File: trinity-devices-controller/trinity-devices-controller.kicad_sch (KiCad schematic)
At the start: 90 parts, among them IC1 LM25145RGYR, IC2 MCP2562, J1 xh2pin, J10 xh2pin, J11 Conn_01x03, J12 Conn_01x03, J13 Conn_01x03, J2 xh2pin, J3 Conn_01x01_Pin, J4 Conn_01x01_Pin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

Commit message: 配置、配線完了
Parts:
- added C32: 0.1uf, Capacitor_SMD:C_0603_1608Metric_Pad1.08x0.95mm_HandSolder, symbol Device:C
- added D10, D11, D12, D5, D6, D7, D8, D9: LED, LED_SMD:LED_0603_1608Metric_Pad1.05x0.95mm_HandSolder, symbol Device:LED
- added J14: Conn_01x02, Connector_AMASS:AMASS_XT30UPB-M_1x02_P5.0mm_Vertical, symbol Connector_Generic:Conn_01x02
- added J15: Conn_01x03, Connector_JST:JST_XH_B3B-XH-A_1x03_P2.50mm_Vertical, symbol Connector_Generic:Conn_01x03
- added R27, R28, R29, R30, R31: 10k, Resistor_SMD:R_0603_1608Metric_Pad0.98x0.95mm_HandSolder, symbol Device:R
- added R32, R33, R34, R35, R36, R37, R38, R39: 1k, Resistor_SMD:R_0603_1608Metric_Pad0.98x0.95mm_HandSolder, symbol Device:R
- J1, J10, J2, J9: footprint Connector_JST:JST_XH_S2B-XH-A_1x02_P2.50mm_Horizontal -> Connector_JST:JST_XH_B2B-XH-A_1x02_P2.50mm_Vertical
- J11, J12, J13: footprint Connector_JST:JST_XH_S3B-XH-A_1x03_P2.50mm_Horizontal -> Connector_JST:JST_XH_B3B-XH-A_1x03_P2.50mm_Vertical
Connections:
- net +12V: now also J11.2 (Pin_2), J12.2 (Pin_2), J13.2 (Pin_2), J14.2 (Pin_2), J15.2 (Pin_2); no longer J11.3 (Pin_3), J12.3 (Pin_3), J13.3 (Pin_3)
- net GND: now also C32.2, J14.1 (Pin_1), J15.1 (Pin_1), R27.1, R28.1, R29.1, R30.1
- net GNDD: now also D10.1 (K), D11.1 (K), D12.1 (K), D5.1 (K), D6.1 (K), D7.1 (K), D8.1 (K), D9.1 (K), R31.2
- net IN1: now also U3.10 (PA5), R32.1; no longer U3.9 (PA4)
- net IN2: now also U3.9 (PA4), R33.1; no longer U3.10 (PA5)
- net IN3: now also R34.1
- net IN4: now also R35.1
- net PWM1: now also J11.3 (Pin_3), U8.11 (OUTD), R27.2; no longer J11.2 (Pin_2), U8.14 (OUTA)
- net PWM2: now also J12.3 (Pin_3), U8.12 (OUTC), R28.2; no longer J12.2 (Pin_2), U8.13 (OUTB)
- net PWM3: now also J13.3 (Pin_3), U8.13 (OUTB), R29.2; no longer J13.2 (Pin_2), U8.12 (OUTC)
- net TIM2_CH1: now also U8.6 (IND), R31.1, R39.1; no longer R26.1, U8.3 (INA)
- net TIM2_CH2: now also R24.1, U8.5 (INC), R38.1; no longer R25.1, U8.4 (INB)
- net TIM2_CH3: now also R25.1, U8.4 (INB), R37.1; no longer R24.1, U8.5 (INC)
- net VCC: now also C32.1
- net at R18.2: now also U1.3; no longer U1.5
- net at R3.1, R5.1: now also U1.11; no longer U1.15
- net at R2.2: now also U1.7; no longer U1.3
- net at R4.1, R6.1: now also U1.9; no longer U1.13
- net at U1.1: now also R21.2; no longer R1.2
- net at R19.1, R20.1: now also U1.13; no longer U1.11
- net at C3.2, C5.1, IC1.5 (FB)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: now also R14.2; no longer C6.2
- net at C5.2, IC1.4 (COMP): now also C6.1; no longer R14.1
- net TIM2_CH4: now reaches U3.8 (PA3)
- net TIM2_CH4: now also R26.1, U8.3 (INA), R36.1
- net at R22.1, R23.1: now also U1.15; no longer U1.9
- new net: D8.2 (A), R35.2
- new net: D5.2 (A), R32.2
- new net: D6.2 (A), R33.2
- new net: D10.2 (A), R37.2
- new net: D11.2 (A), R38.2
- new net: D7.2 (A), R34.2
- new net: C6.2, R14.1
- new net: D9.2 (A), R36.2
- new net: D12.2 (A), R39.2
- new net: R1.2, U1.5
- new net PWM4: J15.3 (Pin_3), R30.2, U8.14 (OUTA)
- no-connect marks 17 -> 14
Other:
- note added: "電源入出力"
- note removed: "電源入力"
- moved on the sheet: C6, J11, J12, J13, J3, J4, R14, R24, R25, R26, U1A, U1B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

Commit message: ビア以外完成
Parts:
- added D13, D14, D15, D16, D17: LED, LED_SMD:LED_0603_1608Metric_Pad1.05x0.95mm_HandSolder, symbol Device:LED
- added R40, R41, R42, R43, R44: 1k, Resistor_SMD:R_0603_1608Metric_Pad0.98x0.95mm_HandSolder, symbol Device:R
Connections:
- net +12V: now also R40.1
- net +3.3V: now also R43.1
- net +5P: now also R41.1
- net +5V: now also R44.1
- net GND: now also D13.1 (K), D14.1 (K), D15.1 (K)
- net GNDD: now also D16.1 (K), D17.1 (K)
- net VCC: now also R42.1
- new net: D15.2 (A), R42.2
- new net: D17.2 (A), R44.2
- new net: D16.2 (A), R43.2
- new net: D13.2 (A), R40.2
- new net: D14.2 (A), R41.2
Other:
- note added: "LED"
- moved on the sheet: D10, D11, D12, D5, D6, D7, D8, D9, J5, J6, J7, J8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

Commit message: 完成、ガーバー作成完了
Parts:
- added D18, D19, D20, D21: LED, LED_SMD:LED_0603_1608Metric_Pad1.05x0.95mm_HandSolder, symbol Device:LED
- added R45, R46, R47, R48: 1k, Resistor_SMD:R_0603_1608Metric_Pad0.98x0.95mm_HandSolder, symbol Device:R
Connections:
- net GNDD: now also D18.1 (K), D19.1 (K), D20.1 (K), D21.1 (K)
- net LED4: now reaches U3.18 (PA8)
- net LED4: now also R48.1
- net LED3: now reaches U3.19 (PA9)
- net LED3: now also R47.1
- net LED2: now reaches U3.20 (PA10)
- net LED2: now also R46.1
- net LED1: now reaches U3.28 (PB5)
- net LED1: now also R45.1
- new net: D21.2 (A), R48.2
- new net: D20.2 (A), R47.2
- new net: D18.2 (A), R45.2
- new net: D19.2 (A), R46.2
- no-connect marks 14 -> 10

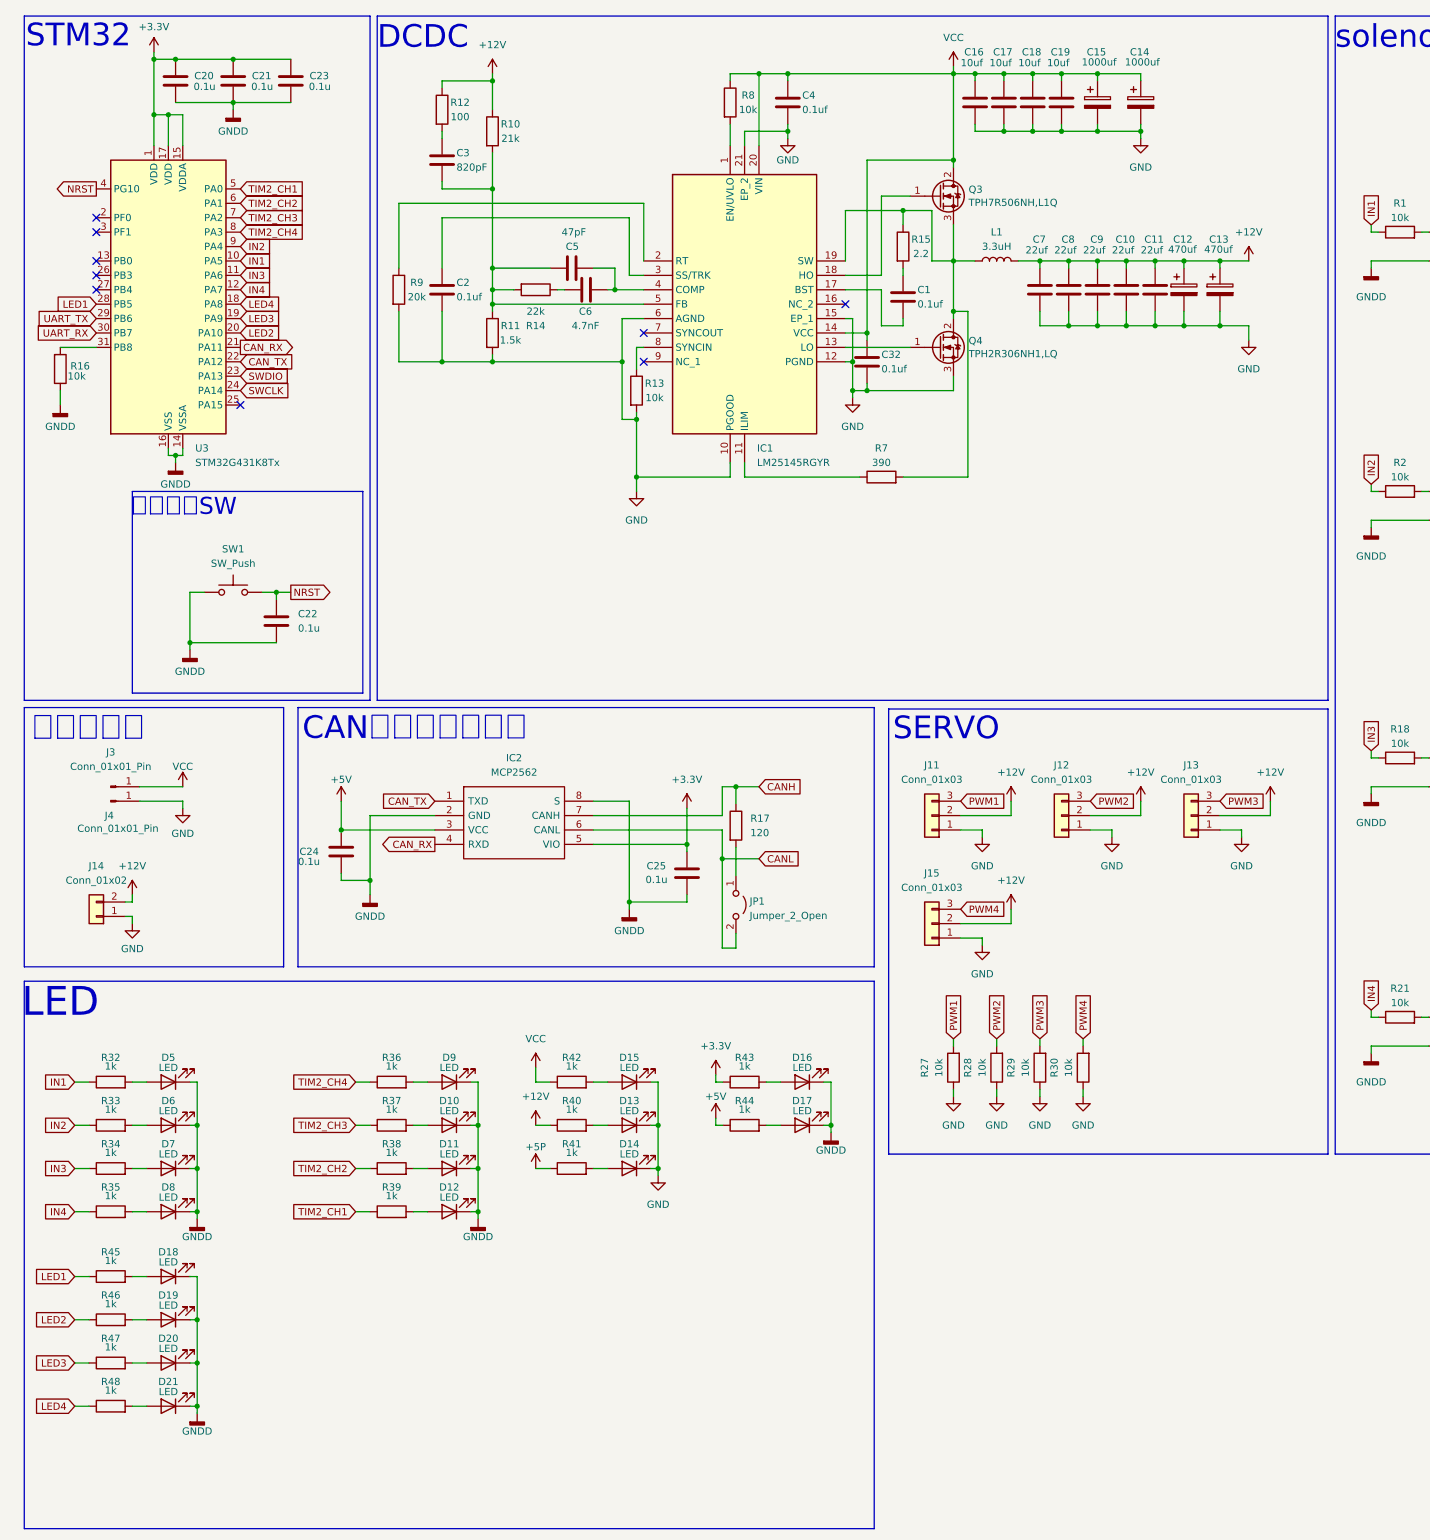
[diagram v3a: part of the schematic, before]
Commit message: VCCのトラブル修正、仕様の一部を変更
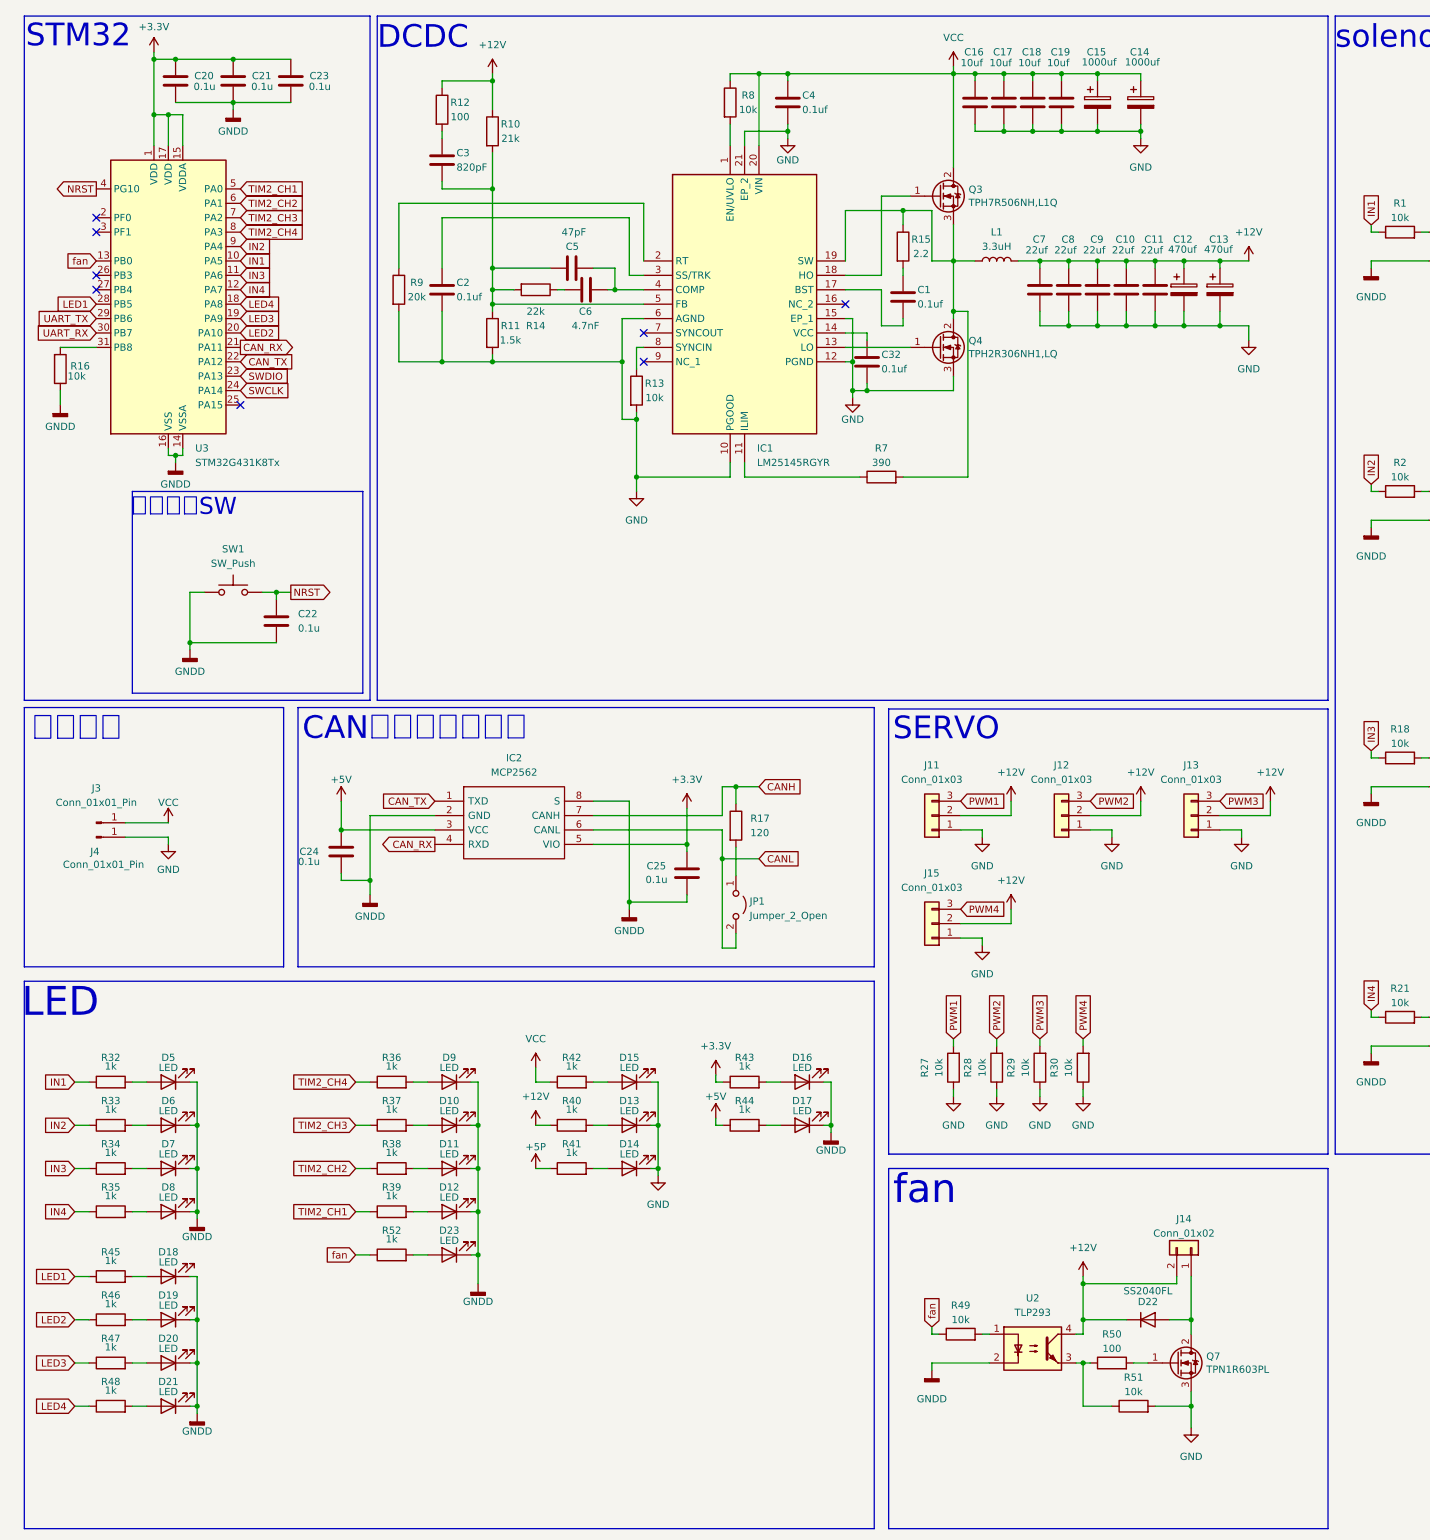
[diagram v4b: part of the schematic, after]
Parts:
- added D22: SS2040FL, 0Ikedalibrary:SOD-123FL, symbol Device:D
- added D23: LED, LED_SMD:LED_0603_1608Metric_Pad1.05x0.95mm_HandSolder, symbol Device:LED
- added Q7: TPN1R603PL, 0Ikedalibrary:TSON Advance, symbol Device:Q_NMOS_GDS
- added R49, R51: 10k, Resistor_SMD:R_0603_1608Metric_Pad0.98x0.95mm_HandSolder, symbol Device:R
- added R50: 100, Resistor_SMD:R_0603_1608Metric_Pad0.98x0.95mm_HandSolder, symbol Device:R
- added R52: 1k, Resistor_SMD:R_0603_1608Metric_Pad0.98x0.95mm_HandSolder, symbol Device:R
- added U2: TLP293, Package_SO:SOIC-4_4.55x2.6mm_P1.27mm, symbol Isolator:TLP293
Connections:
- net +12V: now also D22.1 (K), U2.4
- net GND: now also Q7.3 (S), R51.2; no longer J14.1 (Pin_1)
- net GNDD: now also D23.1 (K), U2.2
- net VCC: no longer C32.1, IC1.14 (VCC)
- net fan: now reaches U3.13 (PB0)
- net fan: now also R49.1, R52.1
- new net: R49.2, U2.1
- new net: R50.1, R51.1, U2.3
- new net: D23.2 (A), R52.2
- new net: C32.1, IC1.14 (VCC)
- new net: Q7.1 (G), R50.2
- new net: D22.2 (A), J14.1 (Pin_1), Q7.2 (D)
- no-connect marks 10 -> 9
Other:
- note added: "fan"
- note added: "電源入力"
- note removed: "電源入出力"
- moved on the sheet: J14, J3, J4

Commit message: 電磁弁の個数変更
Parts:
- added D24, D25, D26: LED, LED_SMD:LED_0603_1608Metric_Pad1.05x0.95mm_HandSolder, symbol Device:LED
- added D27, D28, D29, D30: SS2040FL, 0Ikedalibrary:SOD-123FL, symbol Device:D
- added J16, J17, J18, J19: xh2pin, Connector_JST:JST_XH_B2B-XH-A_1x02_P2.50mm_Vertical, symbol xh2pin:xh2pin
- added Q10, Q11, Q8, Q9: IRFML8244TRPBFTR, Package_TO_SOT_SMD:SOT-23, symbol Transistor_FET:AO3400A
- added R53, R54, R55: 1k, Resistor_SMD:R_0603_1608Metric_Pad0.98x0.95mm_HandSolder, symbol Device:R
- added R56, R57, R58, R59, R64, R65, R66, R67: 10k, Resistor_SMD:R_0603_1608Metric_Pad0.98x0.95mm_HandSolder, symbol Device:R
- added R60, R61, R62, R63: 100, Resistor_SMD:R_0603_1608Metric_Pad0.98x0.95mm_HandSolder, symbol Device:R
- added U5: TLP293-4, Package_SO:SOIC-16_4.55x10.3mm_P1.27mm, symbol Isolator:TLP293-4
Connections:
- net +12V: now also D27.1 (K), D28.1 (K), D29.1 (K), D30.1 (K), J16.2, J17.2, J18.2, J19.2, U5.10, U5.12, U5.14, U5.16
- net GND: now also Q10.2 (S), Q11.2 (S), Q8.2 (S), Q9.2 (S), R64.2, R65.2, R66.2, R67.2
- net GNDD: now also D24.1 (K), D25.1 (K), D26.1 (K), U5.2, U5.4, U5.6, U5.8
- net IN1: now also U3.9 (PA4); no longer U3.10 (PA5)
- net IN2: now also U3.10 (PA5); no longer U3.9 (PA4)
- net LED1: now also U3.27 (PB4); no longer U3.28 (PB5)
- net LED2: now also U3.25 (PA15); no longer U3.20 (PA10)
- net LED3: now also U3.26 (PB3); no longer U3.19 (PA9)
- net at R3.1, R5.1: now also U1.9; no longer U1.11
- net at R2.2: now also U1.5; no longer U1.7
- net at R4.1, R6.1: now also U1.11; no longer U1.9
- net at R1.2: now also U1.7; no longer U1.5
- net LED4 renamed IN5
- net IN5: now also R56.1
- new net: Q11.1 (G), R63.2
- new net: R62.1, R66.1, U5.15
- new net: R59.2, U5.7
- new net: R63.1, R67.1, U5.9
- new net: D25.2 (A), R54.2
- new net: R56.2, U5.5
- new net: R61.1, R65.1, U5.13
- new net: D24.2 (A), R53.2
- new net: Q10.1 (G), R62.2
- new net: R58.2, U5.1
- new net: R57.2, U5.3
- new net: Q9.1 (G), R61.2
- new net: Q8.1 (G), R60.2
- new net: D26.2 (A), R55.2
- new net: R60.1, R64.1, U5.11
- new net IN6: R53.1, R57.1, U3.19 (PA9)
- new net IN7: R54.1, R58.1, U3.20 (PA10)
- new net IN8: R55.1, R59.1, U3.28 (PB5)
- new net OUT5: D27.2 (A), J16.1, Q8.3 (D)
- new net OUT6: D28.2 (A), J17.1, Q9.3 (D)
- new net OUT7: D29.2 (A), J18.1, Q10.3 (D)
- new net OUT8: D30.2 (A), J19.1, Q11.3 (D)
- no-connect marks 9 -> 6
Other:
- moved on the sheet: C26, C27, C28, C29, C30, C31, J5, J6, J7, J8, R24, R25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

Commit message: シルク、ビアの修正
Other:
- moved on the sheet: C26, C27, C28, C29, C30, C31, D10, D11, D12, D13, D14, D15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
